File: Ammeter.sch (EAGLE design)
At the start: 29 parts, among them IC1 ICL7107, IC2 TL081P, IC3 TL081P, IC4 TL081P, IC5 TL081P, IC6 TL081P, IC7 TL081P, IC8 TL081P, IC9 TL081P, T1 BD139

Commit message: Lib: adding 0-10V signal
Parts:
- added IC10, IC11, IC12: TL081P, linear:TL081P
- added R10: 20k, resistor:R-EU_0204/7
- added R11, R23, R24, R8: 1M, resistor:R-EU_0204/7
- added R12: 0.1, resistor:R-EU_0204/7
- added R13, R14: 300, resistor:R-EU_0204/7
- added R15, R16, R17, R18, R21: 15k, resistor:R-EU_0204/7
- added R19: 16k, resistor:R-EU_0204/7
- added R20: (no value), rcl:POTENTIOMETER_PT_SPIN
- added R22: 10k, resistor:R-EU_0204/7
- added R6: 43k, resistor:R-EU_0204/7
- added R7: 4k7, resistor:R-EU_0204/7
- added R9: 82k, resistor:R-EU_0204/7
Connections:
- removed net V+: D1.C, R3.2
- removed net V-: C1.1, C2.2, D1.A, G1.+, G2.-, R2.1
- new net +12V: D1.C, IC10.V+, IC11.V+, IC12.V+, IC2.V+, IC8.V+, R3.2
- new net -12V: C1.1, C2.2, D1.A, G1.+, G2.-, IC10.V-, IC11.V-, IC12.V-, IC2.V-, IC8.V-, R2.1
- new net 0-10V: IC11.OUT, R20.3, R21.2
- new net 0.5-10V: IC2.OUT, R15.1, R18.2
- new net 0.5V: IC8.OUT, R17.2, R8.2
- new net 1V: IC10.OUT, R11.2
- new net IN+: R12.2, R13.2
- new net IN-: R12.1, R14.2
- new net N$11: IC10.-IN, R11.1
- new net N$12: IC8.+IN, R6.1, R7.2
- new net N$13: IC10.+IN, R10.2, R9.1
- new net N$14: IC2.+IN, R13.1, R16.2
- new net N$15: IC2.-IN, R14.1, R15.2
- new net N$16: IC11.-IN, R17.1, R20.1
- new net N$17: IC12.+IN, R21.1, R22.2
- new net N$18: IC11.+IN, R18.1, R19.2
- new net N$19: IC12.-IN, R23.1
- new net N$20: IC12.OUT, R23.2, R24.1
- new net N$7: IC8.-IN, R8.1
- net +5V: now also R6.2, R9.2
- net GND: now also R10.1, R16.1, R19.1, R20.2, R22.1, R7.1
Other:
- moved on the sheet: IC2, IC8

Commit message: Lib: Adding 4-20mA signal
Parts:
- removed IC3, IC4, IC5, IC6, IC7, IC9: TL081P, linear:TL081P
- removed R1: (no value), pot:TRIM_EU-3223G
- added IC13, IC14, IC15: TL081P, linear:TL081P
- added J1: (no value), jumper:SJ
- added R25, R26, R27: 560, resistor:R-EU_0204/7
- added R29: (no value), rcl:POTENTIOMETER_PT_SPIN
- R24: value 1M -> 560
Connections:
- new net N$21: IC14.+IN, R24.2, R25.2
- new net N$22: IC15.OUT, T1.B
- new net N$23: IC14.-IN, R26.2, R27.1
- new net N$24: IC14.OUT, IC15.+IN, R27.2
- new net N$25: IC15.-IN, R29.2, T1.E
- new net N$27: J1.1, T1.C
- net +12V: now also IC13.V+, IC14.V+, IC15.V+, J1.2
- net -12V: now also IC13.V-, IC14.V-, IC15.V-
- net 1V: now also R24.1
- net GND: now also R26.1, R29.1, R29.3
- net N$20: now also R25.1; no longer R24.1
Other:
- note added: "GŁÓWNE ZASILANIE"
- note added: "STABILIZOWANE 5V"
- note added: "STEROWNIK WYŚWIETLACZA"
- note added: "SYGNAL 0-10V"
- note added: "SYGNAL 4-20mA"
- moved on the sheet: IC10, IC11, IC12, IC2, IC8, R10, R11, R12, R13, R14, R15, R16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

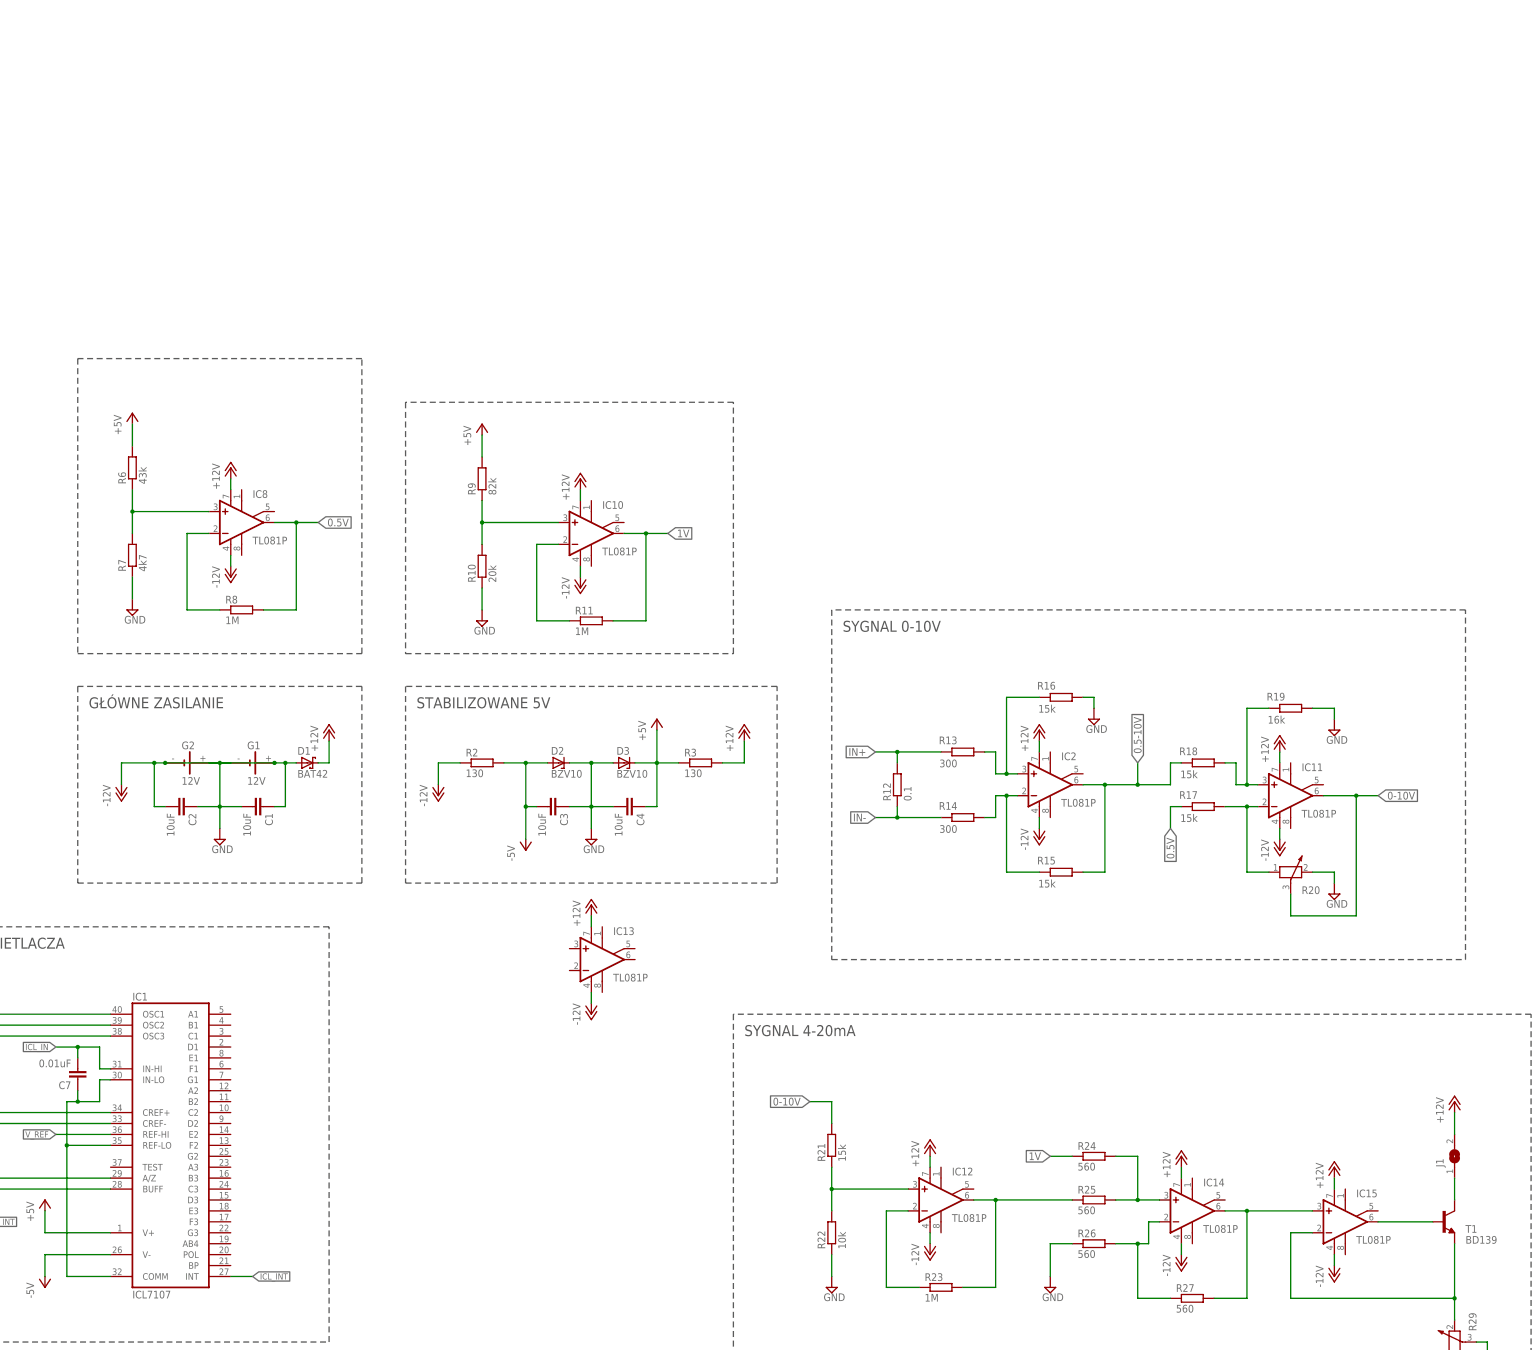
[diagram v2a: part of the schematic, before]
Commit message: Lib: added ICL pins labels and displays
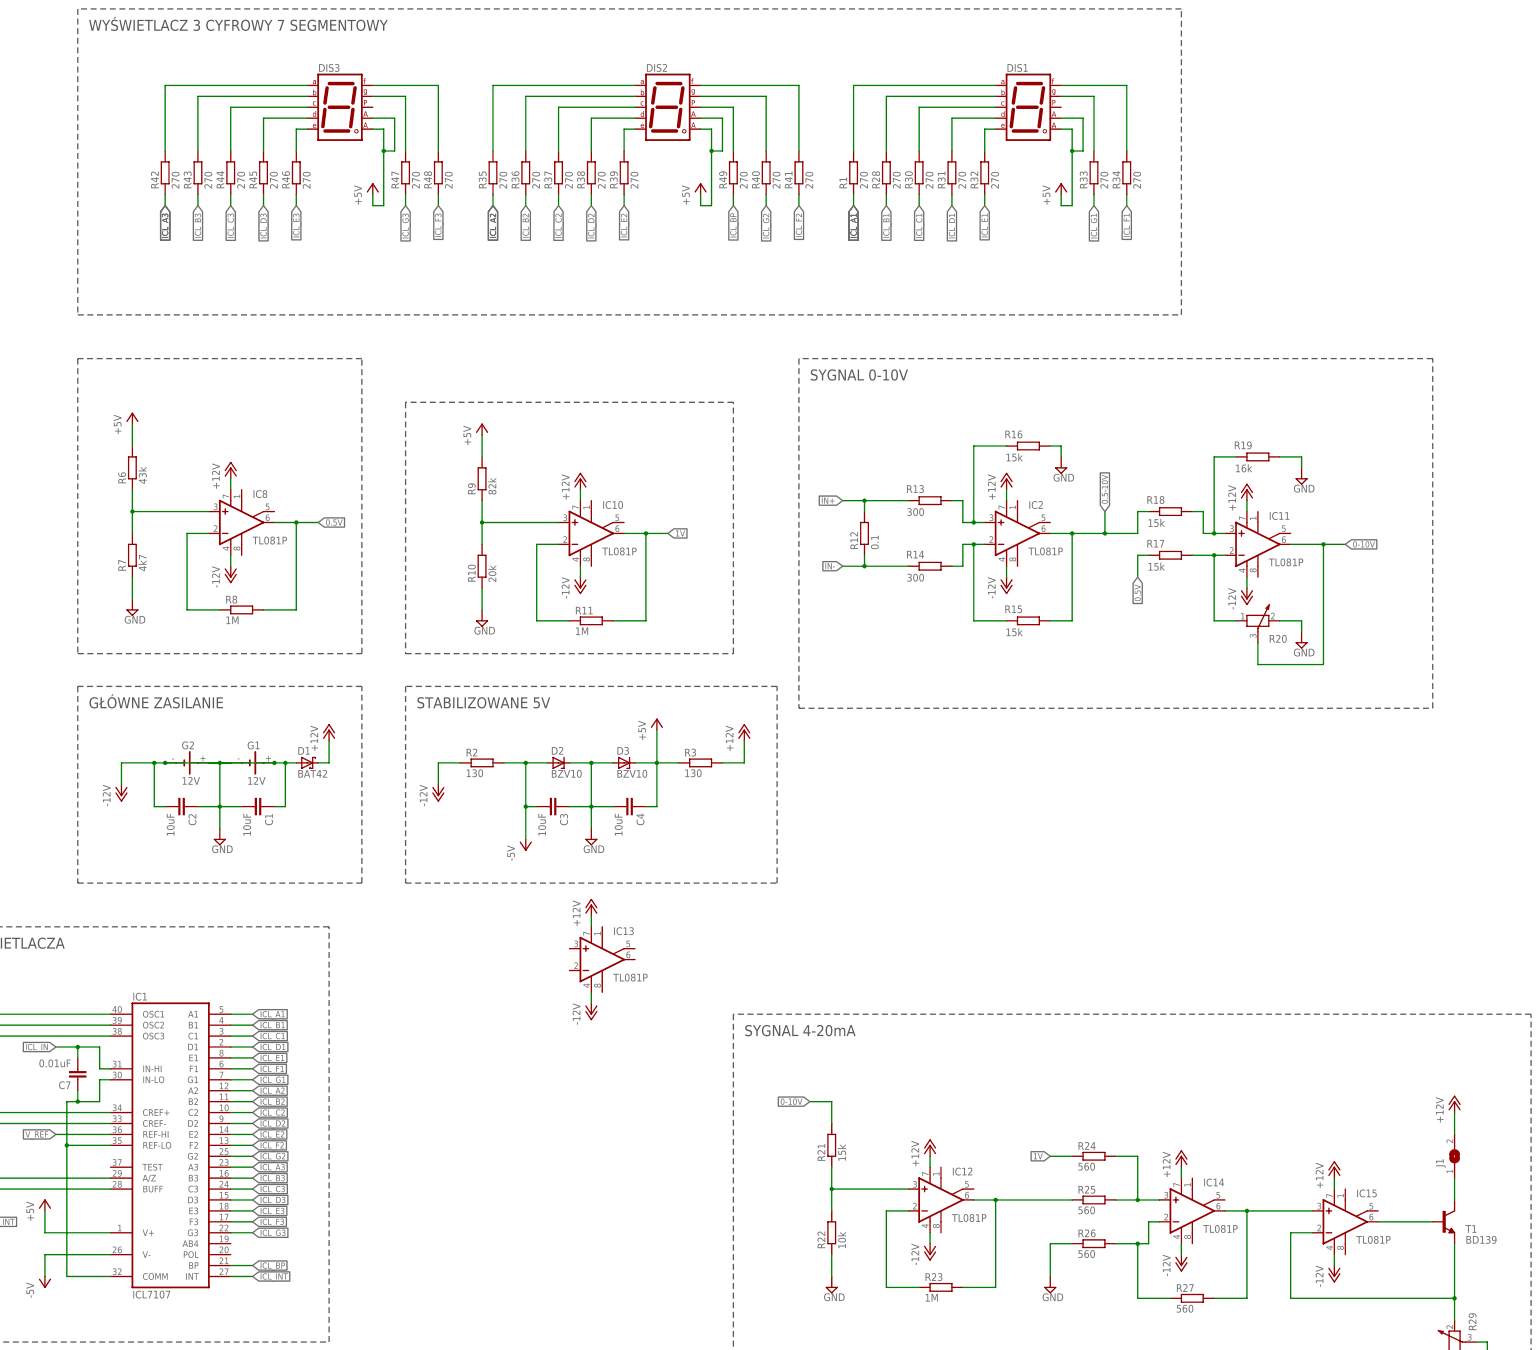
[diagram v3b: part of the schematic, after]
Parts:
- added DIS1, DIS2, DIS3: (no value), special:7SEG-CA
- added R1, R28, R30, R31, R32, R33, R34, R35, R36, R37, R38, R39, R40, R41, R42, R43, R44, R45, R46, R47, R48, R49: 270, resistor:R-EU_0204/7
- T1: SPICEPREFIX (none) -> J
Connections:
- new net ICL_A1: IC1.A1, R1.1
- new net ICL_A2: IC1.A2, R35.1
- new net ICL_A3: IC1.A3, R42.1
- new net ICL_B1: IC1.B1, R28.1
- new net ICL_B2: IC1.B2, R36.1
- new net ICL_B3: IC1.B3, R43.1
- new net ICL_BP: IC1.BP, R49.1
- new net ICL_C1: IC1.C1, R30.1
- new net ICL_C2: IC1.C2, R37.1
- new net ICL_C3: IC1.C3, R44.1
- new net ICL_D1: IC1.D1, R31.1
- new net ICL_D2: IC1.D2, R38.1
- new net ICL_D3: IC1.D3, R45.1
- new net ICL_E1: IC1.E1, R32.1
- new net ICL_E2: IC1.E2, R39.1
- new net ICL_E3: IC1.E3, R46.1
- new net ICL_F1: IC1.F1, R34.1
- new net ICL_F2: IC1.F2, R41.1
- new net ICL_F3: IC1.F3, R48.1
- new net ICL_G1: IC1.G1, R33.1
- new net ICL_G2: IC1.G2, R40.1
- new net ICL_G3: IC1.G3, R47.1
- new net N$26: DIS1.A, R1.2
- new net N$28: DIS1.B, R28.2
- new net N$29: DIS1.C, R30.2
- new net N$30: DIS1.D, R31.2
- new net N$31: DIS1.E, R32.2
- new net N$32: DIS1.F, R34.2
- new net N$33: DIS2.A, R35.2
- new net N$34: DIS1.G, R33.2
- new net N$35: DIS2.D, R38.2
- new net N$36: DIS2.B, R36.2
- new net N$37: DIS2.C, R37.2
- new net N$38: DIS2.E, R39.2
- new net N$39: DIS2.F, R41.2
- new net N$40: DIS2.G, R40.2
- new net N$41: DIS3.A, R42.2
- new net N$42: DIS3.D, R45.2
- new net N$43: DIS3.B, R43.2
- new net N$44: DIS3.C, R44.2
- new net N$45: DIS3.E, R46.2
- new net N$46: DIS3.F, R48.2
- new net N$47: DIS3.G, R47.2
- new net N$48: DIS2.DP, R49.2
- net +5V: now also DIS1.CA1, DIS1.CA2, DIS2.CA1, DIS2.CA2, DIS3.CA1, DIS3.CA2
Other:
- note added: "WYŚWIETLACZ 3 CYFROWY 7 SEGMENTOWY"
- moved on the sheet: IC11, IC2, R12, R13, R14, R15, R16, R17, R18, R19, R20

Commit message: Added ICL_IN signal, renumbered parts
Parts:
- removed D2: BZV10, diode:BZV10
- removed IC10, IC11, IC12, IC13, IC14, IC15: TL081P, linear:TL081P
- removed J1: (no value), jumper:SJ
- added D4: BAT42, diode:BAS40
- added IC3: ICL7107, ICL7107:ICL7107
- added IC4, IC5, IC6, IC7, IC9: TL081P, linear:TL081P
- added R50, R53: (no value), rcl:POTENTIOMETER_PT_SPIN
- added R51, R52: 2k, resistor:R-EU_0204/7
- added SJ1: (no value), jumper:SJ
- C7: value 0.01uF -> 0.047uF
- C8: value 0.047uF -> 0.22uF
- C9: value 0.22uF -> 0.01uF
- D1: value BAT42 -> BZV10; device diode:BAS40 -> diode:BZV10
- IC1: value ICL7107 -> TL081P; device ICL7107:ICL7107 -> linear:TL081P
- R10: value 20k -> 270
- R11: value 1M -> 130
- R12: value 0.1 -> 270
- R13: value 300 -> 270
- R14: value 300 -> 82k
- R15: value 15k -> 20k
- R16, R17, R18: value 15k -> 270
- R19: value 16k -> 1M
- R2: value 130 -> 43k
- R20: value (none) -> 100k; device rcl:POTENTIOMETER_PT_SPIN -> resistor:R-EU_0204/7
- R21: value 15k -> 470k
- R22: value 10k -> 270
- R23: value 1M -> 270
- R24, R25, R26, R27: value 560 -> 270
- R29: value (none) -> 270; device rcl:POTENTIOMETER_PT_SPIN -> resistor:R-EU_0204/7
- R3: value 130 -> 4k7
- R33, R42, R43, R47, R48: value 270 -> 15k
- R34: value 270 -> 10k
- R35: value 270 -> 1M
- R36: value 270 -> 0.1
- R37, R38: value 270 -> 300
- R39, R40, R41, R44: value 270 -> 560
- R4: value 100k -> 270
- R45, R46: value 270 -> 100k
- R49: value 270 -> 16k
- R5: value 470k -> 130
- R6: value 43k -> 270
- R7: value 4k7 -> 270
- R9: value 82k -> 270
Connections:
- new net N$49: IC9.+IN, R45.2, R51.1
- new net N$51: IC9.-IN, R46.2, R52.1
- net +12V: now also D4.C, IC1.V+, IC4.V+, IC5.V+, IC6.V+, IC7.V+, IC9.V+, R11.2, SJ1.2; no longer D1.C, IC10.V+, IC11.V+, IC12.V+, IC13.V+, IC14.V+, IC15.V+, J1.2, R3.2
- net +5V: now also IC3.V+, R11.1, R14.2, R2.2; no longer IC1.V+, R3.1, R6.2, R9.2
- net -12V: now also C1.2, C3.1, D4.A, G1.-, G2.+, IC1.V-, IC4.V-, IC5.V-, IC6.V-, IC7.V-, IC9.V-, R5.1; no longer C1.1, C2.2, D1.A, G1.+, G2.-, IC10.V-, IC11.V-, IC12.V-, IC13.V-, IC14.V-, IC15.V-, R2.1
- net -5V: now also C2.2, D1.A, IC3.V-, R5.2; no longer C3.2, D2.A, IC1.V-, R2.2
- net 0-10V: now also IC8.OUT, R33.2, R50.3; no longer IC11.OUT, R20.3, R21.2
- net 0.5-10V: now also IC5.OUT, R43.1, R45.1, R47.2; no longer IC2.OUT, R15.1, R18.2
- net 0.5V: now also IC1.OUT, R48.2; no longer IC8.OUT, R17.2
- net 1V: now also IC2.OUT, R19.2, R39.1; no longer IC10.OUT, R11.2, R24.1
- net GND: now also C1.1, C3.2, D1.C, G1.+, G2.-, R15.1, R3.1, R34.1, R41.1, R42.1, R46.1, R49.1, R50.2, R51.2, R53.1, R53.3; no longer C1.2, C3.1, D2.C, G1.-, G2.+, R10.1, R16.1, R19.1, R20.2, R22.1, R26.1, R29.1, R29.3, R7.1
- net ICL_A1: now also IC3.A1, R26.1; no longer IC1.A1, R1.1
- net ICL_A2: now also IC3.A2, R13.1; no longer IC1.A2, R35.1
- net ICL_A3: now also IC3.A3, R1.1; no longer IC1.A3, R42.1
- net ICL_B1: now also IC3.B1, R27.1; no longer IC1.B1, R28.1
- net ICL_B2: now also IC3.B2, R16.1; no longer IC1.B2, R36.1
- net ICL_B3: now also IC3.B3, R4.1; no longer IC1.B3, R43.1
- net ICL_BP: now also IC3.BP, R23.1; no longer IC1.BP, R49.1
- net ICL_C1: now also IC3.C1, R28.1; no longer IC1.C1, R30.1
- net ICL_C2: now also IC3.C2, R17.1; no longer IC1.C2, R37.1
- net ICL_C3: now also IC3.C3, R6.1; no longer IC1.C3, R44.1
- net ICL_D1: now also IC3.D1, R29.1; no longer IC1.D1, R31.1
- net ICL_D2: now also IC3.D2, R18.1; no longer IC1.D2, R38.1
- net ICL_D3: now also IC3.D3, R7.1; no longer IC1.D3, R45.1
- net ICL_E1: now also IC3.E1, R30.1; no longer IC1.E1, R32.1
- net ICL_E2: now also IC3.E2, R22.1; no longer IC1.E2, R39.1
- net ICL_E3: now also IC3.E3, R9.1; no longer IC1.E3, R46.1
- net ICL_F1: now also IC3.F1, R32.1; no longer IC1.F1, R34.1
- net ICL_F2: now also IC3.F2, R25.1; no longer IC1.F2, R41.1
- net ICL_F3: now also IC3.F3, R12.1; no longer IC1.F3, R48.1
- net ICL_G1: now also IC3.G1, R31.1; no longer IC1.G1, R33.1
- net ICL_G2: now also IC3.G2, R24.1; no longer IC1.G2, R40.1
- net ICL_G3: now also IC3.G3, R10.1; no longer IC1.G3, R47.1
- net ICL_IN: now also C9.2, IC3.IN-HI, IC9.OUT, R52.2; no longer C7.2, IC1.IN-HI
- net ICL_INT: now also IC3.INT; no longer IC1.INT
- net ILC_INT: now also C8.1; no longer C9.1
- net IN+: now also R36.2, R37.2; no longer R12.2, R13.2
- net IN-: now also R36.1, R38.2; no longer R12.1, R14.2
- net N$1: now also IC3.OSC1, R20.1; no longer IC1.OSC1, R4.1
- net N$10: now also C7.2, R21.1; no longer C9.2, R5.1
- net N$11: now also IC2.-IN, R19.1; no longer IC10.-IN, R11.1
- net N$12: now also IC1.+IN, R2.1, R3.2; no longer IC8.+IN, R6.1, R7.2
- net N$13: now also IC2.+IN, R14.1, R15.2; no longer IC10.+IN, R10.2, R9.1
- net N$14: now also IC5.+IN, R37.1, R42.2; no longer IC2.+IN, R13.1, R16.2
- net N$15: now also IC5.-IN, R38.1, R43.2; no longer IC2.-IN, R14.1, R15.2
- net N$16: now also IC8.-IN, R48.1, R50.1; no longer IC11.-IN, R17.1, R20.1
- net N$17: now also IC4.+IN, R33.1, R34.2; no longer IC12.+IN, R21.1, R22.2
- net N$18: now also IC8.+IN, R47.1, R49.2; no longer IC11.+IN, R18.1, R19.2
- net N$19: now also IC4.-IN, R35.1; no longer IC12.-IN, R23.1
- net N$2: now also IC3.OSC2, R20.2; no longer IC1.OSC2, R4.2
- net N$20: now also IC4.OUT, R35.2, R40.1; no longer IC12.OUT, R23.2, R25.1
- net N$21: now also IC6.+IN, R39.2, R40.2; no longer IC14.+IN, R24.2, R25.2
- net N$22: now also IC7.OUT; no longer IC15.OUT
- net N$23: now also IC6.-IN, R41.2, R44.1; no longer IC14.-IN, R26.2, R27.1
- net N$24: now also IC6.OUT, IC7.+IN, R44.2; no longer IC14.OUT, IC15.+IN, R27.2
- net N$25: now also IC7.-IN, R53.2; no longer IC15.-IN, R29.2
- net N$26: now also R26.2; no longer R1.2
- net N$27: now also SJ1.1; no longer J1.1
- net N$28: now also R27.2; no longer R28.2
- net N$29: now also R28.2; no longer R30.2
- net N$3: now also IC3.OSC3; no longer IC1.OSC3
- net N$30: now also R29.2; no longer R31.2
- net N$31: now also R30.2; no longer R32.2
- net N$32: now also R32.2; no longer R34.2
- net N$33: now also R13.2; no longer R35.2
- net N$34: now also R31.2; no longer R33.2
- net N$35: now also R18.2; no longer R38.2
- net N$36: now also R16.2; no longer R36.2
- net N$37: now also R17.2; no longer R37.2
- net N$38: now also R22.2; no longer R39.2
- net N$39: now also R25.2; no longer R41.2
- net N$4: now also IC3.CREF+; no longer IC1.CREF+
- net N$40: now also R24.2; no longer R40.2
- net N$41: now also R1.2; no longer R42.2
- net N$42: now also R7.2; no longer R45.2
- net N$43: now also R4.2; no longer R43.2
- net N$44: now also R6.2; no longer R44.2
- net N$45: now also R9.2; no longer R46.2
- net N$46: now also R12.2; no longer R48.2
- net N$47: now also R10.2; no longer R47.2
- net N$48: now also R23.2; no longer R49.2
- net N$5: now also C9.1, IC3.COMM, IC3.IN-LO, IC3.REF-LO; no longer C7.1, IC1.COMM, IC1.IN-LO, IC1.REF-LO
- net N$6: now also IC3.CREF-; no longer IC1.CREF-
- net N$7: now also IC1.-IN; no longer IC8.-IN
- net N$8: now also C7.1, IC3.A/Z; no longer C8.1, IC1.A/Z
- net N$9: now also IC3.BUFF, R21.2; no longer IC1.BUFF, R5.2
- net V_REF: now also IC3.REF-HI; no longer IC1.REF-HI
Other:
- note added: "SYGNAL ICL_IN (0.01-0.2V)"
- moved on the sheet: C1, C2, C3, C4, C5, C6, C7, C8, C9, D3, DIS1, DIS2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

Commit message: Added separate power supply for displays, updating parts' values
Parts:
- added C10: 10uF, resistor:C-EU025-024X044
- added D2: BZV10, diode:BZV10
- added R54: 110, resistor:R-EU_0204/7
- R11, R5: value 130 -> 100
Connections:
- removed net N$5: C9.1, IC3.COMM, IC3.IN-LO, IC3.REF-LO
- net +12V: now also R54.2
- net +5V: now also C10.1, D2.C, R54.1
- net GND: now also C10.2, C9.1, D2.A, IC3.COMM, IC3.IN-LO, IC3.REF-LO
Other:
- note added: "ZASILANIE ICL (5V)"
- note added: "ZASILANIE WYŚWIETLACZY (5.6V)"
- note removed: "STABILIZOWANE 5V"

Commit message: Renumbering parts
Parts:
- removed C10: 10uF, resistor:C-EU025-024X044
- removed C9: 0.01uF, resistor:C-EU025-024X044
- removed D4: BAT42, diode:BAS40
- C3: value 10uF -> 100pF
- C4: value 10uF -> 0.1uF
- C5: value 100pF -> 0.047uF
- C6: value 0.1uF -> 0.22uF
- C7: value 0.047uF -> 0.01uF
- C8: value 0.22uF -> 10uF
- D2: SPICEPREFIX D -> (none)
- D3: SPICEPREFIX (none) -> D
- R29: value 270 -> 110
- R33: value 15k -> 270
- R34: value 10k -> 15k
- R35: value 1M -> 10k
- R36: value 0.1 -> 1M
- R37: value 300 -> 0.1
- R39: value 560 -> 300
- R42: value 15k -> 560
- R44: value 560 -> 15k
- R45: value 100k -> 560
- R47: value 15k -> 100k
- R49: value 16k -> 15k
- R50: value (none) -> 16k; device rcl:POTENTIOMETER_PT_SPIN -> resistor:R-EU_0204/7
- R51: value 2k -> (none); device resistor:R-EU_0204/7 -> rcl:POTENTIOMETER_PT_SPIN
- R53: value (none) -> 2k; device rcl:POTENTIOMETER_PT_SPIN -> resistor:R-EU_0204/7
- R54: value 110 -> (none); device resistor:R-EU_0204/7 -> rcl:POTENTIOMETER_PT_SPIN
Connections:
- net +12V: now also G1.-, G2.+, R29.2; no longer D4.C, R54.2
- net +5V: now also C2.1, C8.1, R29.1; no longer C10.1, C4.1, R54.1
- net -12V: no longer C1.2, C3.1, D4.A, G1.-, G2.+
- net -5V: now also C1.2; no longer C2.2
- net 0-10V: now also R34.2, R51.3; no longer R33.2, R50.3
- net 0.5-10V: now also R44.1, R46.1, R48.2; no longer R43.1, R45.1, R47.2
- net 0.5V: now also R49.2; no longer R48.2
- net 1V: now also R40.1; no longer R39.1
- net GND: now also C2.2, C7.1, C8.2, R35.1, R43.1, R47.1, R50.1, R52.2, R54.1, R54.3; no longer C10.2, C2.1, C3.2, C4.2, C9.1, R34.1, R41.1, R46.1, R49.1, R50.2, R53.1, R53.3
- net ICL_D1: now also R30.1; no longer R29.1
- net ICL_E1: now also R31.1; no longer R30.1
- net ICL_F1: now also R33.1; no longer R32.1
- net ICL_G1: now also R32.1; no longer R31.1
- net ICL_IN: now also C7.2, R53.2; no longer C9.2, R52.2
- net ILC_INT: now also C6.1; no longer C8.1
- net IN+: now also R38.2; no longer R36.2
- net IN-: now also R37.1, R39.2; no longer R36.1, R38.2
- net N$1: now also C3.2; no longer C5.2
- net N$10: now also C5.2, C6.2; no longer C7.2, C8.2
- net N$14: now also R38.1, R43.2; no longer R37.1, R42.2
- net N$15: now also R39.1, R44.2; no longer R38.1, R43.2
- net N$16: now also R49.1, R51.1; no longer R48.1, R50.1
- net N$17: now also R34.1, R35.2; no longer R33.1, R34.2
- net N$18: now also R48.1, R50.2; no longer R47.1, R49.2
- net N$19: now also R36.1; no longer R35.1
- net N$20: now also R36.2, R41.1; no longer R35.2, R40.1
- net N$21: now also R41.2; no longer R39.2
- net N$23: now also R42.2, R45.1; no longer R41.2, R44.1
- net N$24: now also R45.2; no longer R44.2
- net N$25: now also R54.2; no longer R53.2
- net N$3: now also C3.1; no longer C5.1
- net N$30: now also R30.2; no longer R29.2
- net N$31: now also R31.2; no longer R30.2
- net N$32: now also R33.2; no longer R32.2
- net N$34: now also R32.2; no longer R31.2
- net N$4: now also C4.2; no longer C6.2
- net N$49: now also R46.2, R52.1; no longer R45.2, R51.1
- net N$51: now also R47.2, R53.1; no longer R46.2, R52.1
- net N$6: now also C4.1; no longer C6.1
- net N$8: now also C5.1; no longer C7.1
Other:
- note added: "NAPIĘCIE REF. (0.5V)"
- note added: "NAPIĘCIE REF. (1V)"
- moved on the sheet: C1, C2, C3, C4, C5, C6, C7, C8, D2, D3, IC9, R29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
